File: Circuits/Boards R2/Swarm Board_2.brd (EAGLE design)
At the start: 54.9 x 63.6 mm, 94 parts, among them CON1 ISP(2X3), CON2 MAIN_CONNECTOR, CON3 FTDI_3PIN, CON4 HEADER_3X1, T1 NPN2N2222, T10 TEFT4300, T11 NPN2N2222, T13 NPN2N2222, T14 NPN2N2222, T15 NPN2N2222, T16 NPN2N2222, T17 NPN2N2222, T18 NPN2N2222, T2 NPN2N2222, T3 NPN2N2222, T4 TEFT4300, T5 TEFT4300, T6 TEFT4300, T7 TEFT4300, T8 TEFT4300, T9 TEFT4300, U1 ATMEGA324P, U2 MCP73833

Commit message: more board updates
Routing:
- net +3V: track 376.1 -> 375.4 mm
- net +VRAW: track 85.2 -> 85.7 mm
- net +VCHG: track 44.9 -> 45.4 mm
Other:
- board size 54.9 x 63.6 mm -> 56.1 x 63.5 mm
- board text added: "11-26-12"
- board text removed: "10-28-12"
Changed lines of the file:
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@@
 <board>
 <plain>
-<wire x1="4.318" y1="47.625" x2="4.318" y2="15.7988" width="0.2032" layer="20"/>
-<wire x1="59.182" y1="47.625" x2="59.182" y2="15.7988" width="0.2032" layer="20"/>
+<wire x1="3.716528125" y1="46.6557375" x2="3.716528125" y2="16.8442625" width="0.2032" layer="20"/>
+<wire x1="59.783471875" y1="46.6557375" x2="59.783471875" y2="16.8442625" width="0.2032" layer="20"/>
 <text x="43.434" y="31.496" size="0.8128" layer="21">RXI</text>
 <text x="43.307" y="34.036" size="0.8128" layer="21">TXO</text>
@@
 <text x="43.307" y="49.022" size="0.6096" layer="21">DATA</text>
 <text x="17.907" y="32.512" size="1.016" layer="21" rot="R90">CHGSTATUS</text>
-<text x="14.097" y="9.144" size="1.27" layer="21">10-28-12</text>
+<text x="14.097" y="9.144" size="1.27" layer="21">11-26-12</text>
 <text x="10.541" y="11.684" size="1.27" layer="21">SwarmBoard V2</text>
 <text x="17.653" y="6.731" size="1.27" layer="21">CPRC</text>
-<wire x1="4.318" y1="47.625" x2="59.182" y2="47.625" width="0.2032" layer="20" curve="-120"/>
-<wire x1="4.318" y1="15.748" x2="59.182" y2="15.748" width="0.2032" layer="20" curve="120"/>
+<wire x1="3.716528125" y1="46.6557375" x2="59.783471875" y2="46.6557375" width="0.2032" layer="20" curve="-124"/>
+<wire x1="3.716528125" y1="16.8442625" x2="59.783471875" y2="16.8442625" width="0.2032" layer="20" curve="124"/>
 <text x="27.051" y="48.387" size="0.8128" layer="22" rot="MR270">B+</text>
 <text x="27.178" y="42.164" size="0.8128" layer="22" rot="MR270">B-</text>
@@
 </class>
 </classes>
-<designrules name="default">
+<designrules name="SparkFunDRC">
 <description language="en">&lt;b&gt;EAGLE Design Rules&lt;/b&gt;
 &lt;p&gt;
@@
 <wire x1="58.039" y1="27.178" x2="58.039" y2="20.066" width="0.4064" layer="16"/>
 <wire x1="58.039" y1="20.066" x2="58.039" y2="15.875" width="0.4064" layer="16"/>
-<wire x1="58.039" y1="15.875" x2="46.355" y2="4.191" width="0.4064" layer="16"/>
-<wire x1="46.355" y1="4.191" x2="33.02" y2="4.064" width="0.4064" layer="16"/>
-<wire x1="33.02" y1="4.064" x2="17.399" y2="4.064" width="0.4064" layer="16"/>
-<wire x1="17.399" y1="4.064" x2="5.7785" y2="15.6845" width="0.4064" layer="16"/>
+<wire x1="58.039" y1="15.875" x2="46.609" y2="4.445" width="0.4064" layer="16"/>
+<wire x1="46.609" y1="4.445" x2="33.02" y2="4.445" width="0.4064" layer="16"/>
+<wire x1="33.02" y1="4.445" x2="17.018" y2="4.445" width="0.4064" layer="16"/>
+<wire x1="17.018" y1="4.445" x2="5.7785" y2="15.6845" width="0.4064" layer="16"/>
 <wire x1="5.7785" y1="15.6845" x2="5.461" y2="16.129" width="0.4064" layer="16"/>
 <wire x1="5.461" y1="16.129" x2="5.461" y2="26.924" width="0.4064" layer="16"/>
@@
 <wire x1="30.722" y1="8.255" x2="32.377" y2="6.35" width="0.254" layer="1"/>
 <wire x1="32.377" y1="6.35" x2="33.02" y2="6.35" width="0.254" layer="1"/>
-<wire x1="33.02" y1="6.35" x2="33.02" y2="4.064" width="0.4064" layer="16"/>
+<wire x1="33.02" y1="6.35" x2="33.02" y2="4.445" width="0.4064" layer="16"/>
 <wire x1="12.4206" y1="22.05485" x2="10.916" y2="20.940478125" width="0.254" layer="1"/>
 <wire x1="10.16" y1="18.542" x2="10.916" y2="20.940478125" width="0.254" layer="1"/>
@@
 <wire x1="10.533" y1="39.616" x2="11.049" y2="39.612" width="0.254" layer="1"/>
 <wire x1="11.049" y1="39.612" x2="12.954" y2="39.612" width="0.254" layer="1"/>
-<wire x1="18.415" y1="26.602" x2="17.2085" y2="26.6065" width="0.4064" layer="1"/>
-<via x="17.2085" y="26.6065" extent="1-16" drill="0.508"/>
+<wire x1="18.415" y1="26.602" x2="17.4625" y2="26.6065" width="0.4064" layer="1"/>
+<via x="17.4625" y="26.6065" extent="1-16" drill="0.508"/>
 <wire x1="18.415" y1="26.602" x2="18.415" y2="28.841" width="0.4064" layer="1"/>
 <contactref element="U$1" pad="18"/>
@@
 <wire x1="16.51" y1="38.227" x2="15.629" y2="39.108" width="0.4064" layer="1"/>
 <wire x1="15.629" y1="39.108" x2="14.859" y2="39.108" width="0.4064" layer="1"/>
-<wire x1="16.155" y1="34.163" x2="18.669" y2="34.163" width="0.4064" layer="1"/>
-<wire x1="18.669" y1="34.163" x2="19.177" y2="34.671" width="0.4064" layer="1"/>
-<wire x1="19.177" y1="34.671" x2="19.177" y2="35.814" width="0.4064" layer="1"/>
-<wire x1="19.177" y1="35.814" x2="18.542" y2="36.449" width="0.4064" layer="1"/>
-<wire x1="18.542" y1="36.449" x2="16.51" y2="36.449" width="0.4064" layer="1"/>
+<wire x1="16.155" y1="34.163" x2="18.923" y2="34.163" width="0.4064" layer="1"/>
+<wire x1="18.923" y1="34.163" x2="19.431" y2="34.671" width="0.4064" layer="1"/>
+<wire x1="19.431" y1="34.671" x2="19.431" y2="35.814" width="0.4064" layer="1"/>
+<wire x1="19.431" y1="35.814" x2="18.796" y2="36.449" width="0.4064" layer="1"/>
+<wire x1="18.796" y1="36.449" x2="16.51" y2="36.449" width="0.4064" layer="1"/>
 <wire x1="14.325" y1="34.813" x2="14.325" y2="35.28" width="0.4064" layer="1"/>
 <wire x1="14.325" y1="35.28" x2="14.605" y2="35.56" width="0.4064" layer="1"/>
@@
 <wire x1="12.827" y1="45.847" x2="15.875" y2="45.847" width="0.254" layer="1"/>
 <wire x1="15.875" y1="45.847" x2="15.875" y2="50.769025" width="0.254" layer="1"/>
-<wire x1="21.082" y1="32.258" x2="19.939" y2="33.401" width="0.254" layer="1"/>
-<wire x1="19.939" y1="33.401" x2="19.939" y2="36.449" width="0.254" layer="1"/>
-<wire x1="19.939" y1="36.449" x2="19.05" y2="37.338" width="0.254" layer="1"/>
-<wire x1="19.05" y1="37.338" x2="19.05" y2="43.307" width="0.254" layer="1"/>
+<wire x1="21.082" y1="32.258" x2="20.066" y2="33.274" width="0.254" layer="1"/>
+<wire x1="20.066" y1="33.274" x2="20.066" y2="42.291" width="0.254" layer="1"/>
+<wire x1="20.066" y1="42.291" x2="19.05" y2="43.307" width="0.254" layer="1"/>
 <wire x1="19.05" y1="43.307" x2="16.51" y2="45.847" width="0.254" layer="16"/>
 <via x="16.51" y="45.847" extent="1-16" drill="0.508"/>
@@
 <wire x1="16.155" y1="34.813" x2="15.517" y2="34.813" width="0.4064" layer="1"/>
 <wire x1="15.517" y1="34.813" x2="15.24" y2="34.663" width="0.254" layer="1"/>
-<wire x1="16.155" y1="33.513" x2="17.548" y2="33.513" width="0.4064" layer="1"/>
-<wire x1="17.548" y1="33.513" x2="18.0375" y2="33.0235" width="0.4064" layer="1"/>
-<wire x1="16.155" y1="34.813" x2="17.541" y2="34.813" width="0.4064" layer="1"/>
-<wire x1="17.541" y1="34.813" x2="18.034" y2="35.306" width="0.4064" layer="1"/>
-<via x="18.034" y="35.306" extent="1-16" drill="0.508"/>
-<wire x1="18.034" y1="35.306" x2="18.0375" y2="34.4135" width="0.4064" layer="16"/>
-<wire x1="18.0375" y1="34.4135" x2="18.0375" y2="33.0235" width="0.4064" layer="16"/>
-<via x="18.0375" y="33.0235" extent="1-16" drill="0.508"/>
-<via x="18.034" y="37.592" extent="1-16" drill="0.508"/>
-<wire x1="18.034" y1="35.306" x2="18.034" y2="37.592" width="0.4064" layer="16"/>
+<wire x1="16.155" y1="33.513" x2="17.802" y2="33.513" width="0.4064" layer="1"/>
+<wire x1="17.802" y1="33.513" x2="18.2915" y2="33.0235" width="0.4064" layer="1"/>
+<wire x1="16.155" y1="34.813" x2="17.795" y2="34.813" width="0.4064" layer="1"/>
+<wire x1="17.795" y1="34.813" x2="18.288" y2="35.306" width="0.4064" layer="1"/>
+<via x="18.288" y="35.306" extent="1-16" drill="0.508"/>
+<wire x1="18.288" y1="35.306" x2="18.2915" y2="34.4135" width="0.4064" layer="16"/>
+<wire x1="18.2915" y1="34.4135" x2="18.2915" y2="33.0235" width="0.4064" layer="16"/>
+<via x="18.2915" y="33.0235" extent="1-16" drill="0.508"/>
+<via x="18.288" y="37.592" extent="1-16" drill="0.508"/>
+<wire x1="18.288" y1="35.306" x2="18.288" y2="37.592" width="0.4064" layer="16"/>
 <wire x1="15.621" y1="41.529" x2="23.622" y2="49.53" width="0.4064" layer="1"/>
-<wire x1="18.034" y1="37.592" x2="18.034" y2="37.846" width="0.4064" layer="1"/>
-<wire x1="18.034" y1="37.846" x2="15.621" y2="40.259" width="0.4064" layer="1"/>
+<wire x1="18.288" y1="37.592" x2="15.621" y2="40.259" width="0.4064" layer="1"/>
 <wire x1="15.621" y1="40.259" x2="15.621" y2="41.529" width="0.4064" layer="1"/>
 <wire x1="23.622" y1="49.53" x2="32.385" y2="49.53" width="0.4064" layer="1"/>
 <wire x1="32.385" y1="49.53" x2="33.528" y2="50.673" width="0.4064" layer="1"/>
 <wire x1="33.528" y1="50.673" x2="39.497" y2="50.673" width="0.4064" layer="1"/>
-<wire x1="18.415" y1="30.341" x2="18.034" y2="30.741" width="0.4064" layer="1"/>
-<wire x1="18.034" y1="30.741" x2="18.0375" y2="33.0235" width="0.4064" layer="1"/>
+<wire x1="18.415" y1="30.341" x2="18.288" y2="30.487" width="0.4064" layer="1"/>
+<wire x1="18.288" y1="30.487" x2="18.2915" y2="33.0235" width="0.4064" layer="1"/>
 <contactref element="U$1" pad="13"/>
 <contactref element="U$1" pad="24"/>

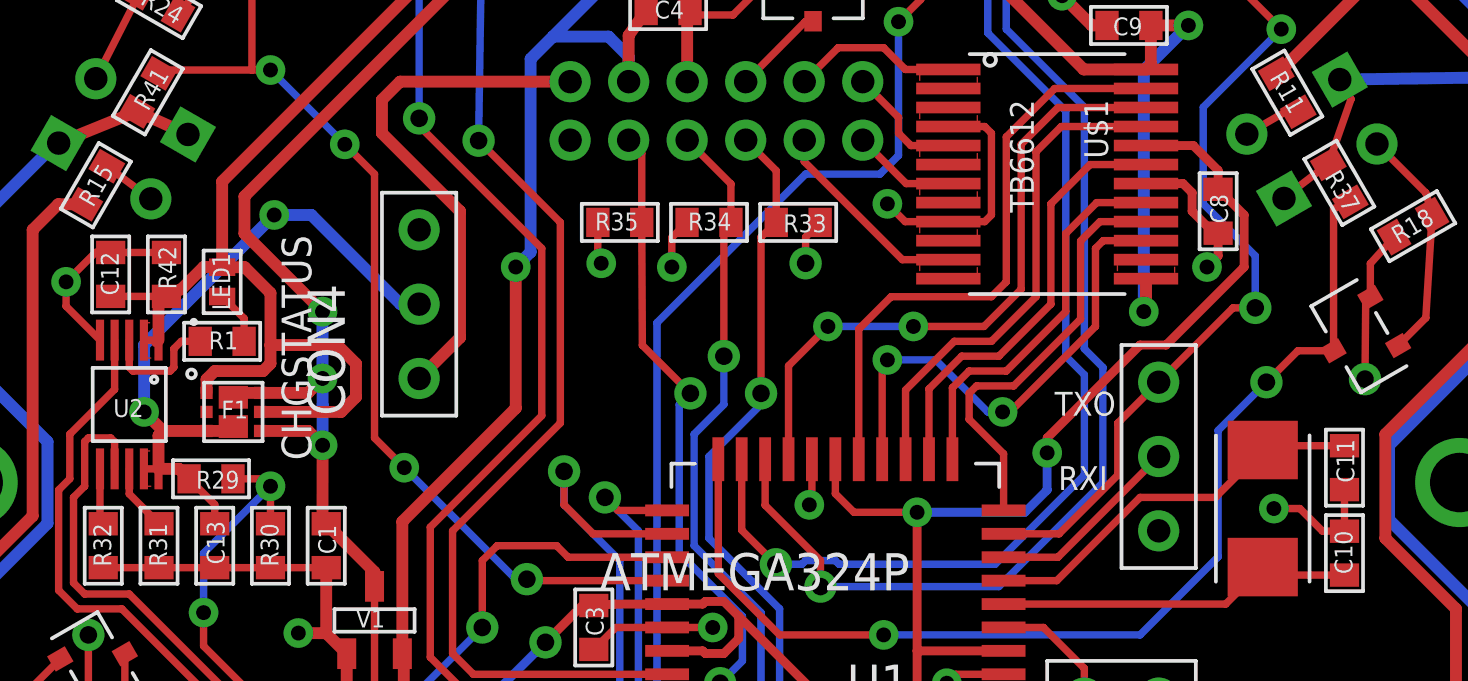
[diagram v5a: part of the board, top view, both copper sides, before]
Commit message: fixed led on swarm board
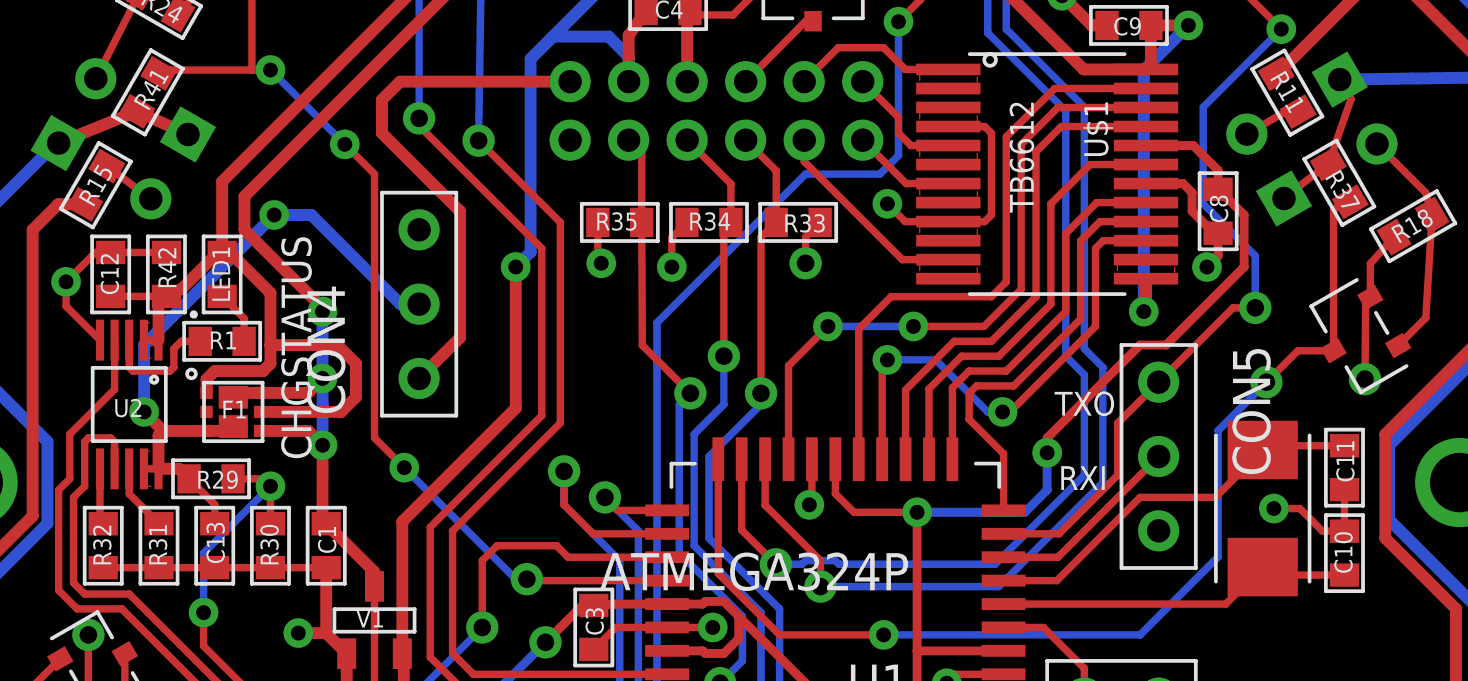
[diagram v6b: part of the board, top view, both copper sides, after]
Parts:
- CON5: value FTDI_3PIN -> HEADER_3X1
- moved LED1 0.25 mm to (14.9, 38.9)
- renumbered CON3 to CON5
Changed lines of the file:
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@@
 <?xml version="1.0" encoding="utf-8"?>
 <!DOCTYPE eagle SYSTEM "eagle.dtd">
-<eagle version="6.3">
+<eagle version="6.2">
 <drawing>
 <settings>
@@
 </class>
 </classes>
-<designrules name="SparkFunDRC">
+<designrules>
 <description language="en">&lt;b&gt;EAGLE Design Rules&lt;/b&gt;
 &lt;p&gt;
@@
 <attribute name="VALUE" x="35.75" y="40.45" size="0.8128" layer="28" rot="MR0"/>
 </element>
-<element name="CON3" library="Mechanical" package="3PINHEADER_.100&quot;" value="FTDI_3PIN" x="46.863" y="32.639" smashed="yes" rot="R270">
-<attribute name="VALUE" x="43.053" y="36.449" size="1.27" layer="27" rot="R270"/>
-</element>
 <element name="T10" library="Passive" package="3MM_LED_RA" value="TEFT4300" x="27.94" y="57.15" smashed="yes"/>
 <element name="R27" library="Passive" package="0603" value="10k" x="30.734" y="55.499" smashed="yes" rot="R270">
@@
 <attribute name="VALUE" x="11.684" y="39.932" size="0.4064" layer="27" rot="R270"/>
 </element>
-<element name="LED1" library="Passive" package="LED0603" value="red" x="14.859" y="38.608" smashed="yes" rot="R90">
-<attribute name="NAME" x="15.132" y="37.638" size="0.6096" layer="25" rot="R90"/>
-<attribute name="VALUE" x="16.129" y="37.538" size="0.4064" layer="27" rot="R90"/>
+<element name="LED1" library="Passive" package="LED0603" value="red" x="14.859" y="38.862" smashed="yes" rot="R90">
+<attribute name="NAME" x="15.132" y="37.892" size="0.6096" layer="25" rot="R90"/>
+<attribute name="VALUE" x="16.129" y="37.792" size="0.4064" layer="27" rot="R90"/>
 </element>
 <element name="R1" library="Passive" package="0603" value="1.5k" x="14.859" y="36.576" smashed="yes">
@@
 <element name="R4" library="Passive" package="0603" value="70" x="21.717" y="17.399" rot="R180"/>
 <element name="R5" library="Passive" package="0603" value="70" x="21.717" y="15.621" rot="R180"/>
+<element name="CON5" library="Mechanical" package="3PINHEADER_.100&quot;" value="HEADER_3X1" x="46.863" y="32.639" rot="R270"/>
 </elements>
 <signals>
@@
 <contactref element="C2" pad="2"/>
 <contactref element="CON1" pad="3"/>
-<contactref element="CON3" pad="3"/>
 <contactref element="T1" pad="2"/>
 <contactref element="R9" pad="1"/>
@@
 <wire x1="48.895" y1="39.497" x2="48.514" y2="39.116" width="0.3048" layer="1"/>
 <wire x1="44.323" y1="25.4" x2="44.323" y2="24.384" width="0.254" layer="1"/>
+<contactref element="CON5" pad="3"/>
 </signal>
 <signal name="+VBAT">
@@
 <wire x1="12.573" y1="36.506" x2="12.684" y2="36.617" width="0.254" layer="1"/>
 <wire x1="12.684" y1="36.617" x2="12.184" y2="36.617" width="0.254" layer="1"/>
-<wire x1="14.597" y1="39.108" x2="14.859" y2="39.108" width="0.254" layer="1"/>
+<wire x1="14.851" y1="39.616" x2="14.859" y2="39.612" width="0.254" layer="1"/>
 <wire x1="23.622" y1="50.8" x2="14.859" y2="42.037" width="0.4064" layer="1"/>
-<wire x1="14.859" y1="42.037" x2="14.859" y2="39.108" width="0.4064" layer="1"/>
+<wire x1="14.859" y1="42.037" x2="14.859" y2="39.612" width="0.4064" layer="1"/>
 <polygon width="0.254" layer="1" thermals="no">
 <vertex x="12.192" y="37.211"/>
@@
 </polygon>
 <wire x1="16.51" y1="36.449" x2="16.51" y2="38.227" width="0.4064" layer="1"/>
-<wire x1="16.51" y1="38.227" x2="15.629" y2="39.108" width="0.4064" layer="1"/>
-<wire x1="15.629" y1="39.108" x2="14.859" y2="39.108" width="0.4064" layer="1"/>
+<wire x1="16.51" y1="38.227" x2="15.121" y2="39.616" width="0.4064" layer="1"/>
+<wire x1="15.121" y1="39.616" x2="14.859" y2="39.612" width="0.4064" layer="1"/>
 <wire x1="16.155" y1="34.163" x2="18.923" y2="34.163" width="0.4064" layer="1"/>
 <wire x1="18.923" y1="34.163" x2="19.431" y2="34.671" width="0.4064" layer="1"/>
@@
 <wire x1="11.049" y1="38.112" x2="12.954" y2="38.112" width="0.254" layer="1"/>
 <wire x1="12.954" y1="38.112" x2="13.47" y2="38.362" width="0.4064" layer="1"/>
-<wire x1="13.47" y1="38.362" x2="14.224" y2="39.116" width="0.4064" layer="1"/>
-<wire x1="14.224" y1="39.116" x2="14.851" y2="39.116" width="0.4064" layer="1"/>
-<wire x1="14.851" y1="39.116" x2="14.859" y2="39.108" width="0.254" layer="1"/>
+<wire x1="13.47" y1="38.362" x2="14.605" y2="39.497" width="0.4064" layer="1"/>
+<wire x1="14.605" y1="39.497" x2="14.724" y2="39.497" width="0.4064" layer="1"/>
+<wire x1="14.724" y1="39.497" x2="14.859" y2="39.612" width="0.254" layer="1"/>
 <wire x1="12.954" y1="38.112" x2="12.684" y2="38.092" width="0.4064" layer="1"/>
 <wire x1="12.684" y1="38.092" x2="12.684" y2="36.617" width="0.4064" layer="1"/>
@@
 <signal name="DATAANTENNA">
 <contactref element="U1" pad="10"/>
-<contactref element="CON3" pad="1"/>
 <contactref element="ANT2" pad="P$1"/>
 <wire x1="41.564" y1="29.997" x2="43.459" y2="29.997" width="0.254" layer="1"/>
@@
 <wire x1="43.459" y1="29.997" x2="45.466" y2="32.004" width="0.254" layer="1"/>
 <wire x1="45.466" y1="32.004" x2="45.466" y2="33.782" width="0.254" layer="1"/>
+<via x="50.165" y="37.719" extent="1-16" drill="0.6"/>
+<wire x1="50.165" y1="37.719" x2="49.657" y2="37.719" width="0.254" layer="1"/>
+<contactref element="CON5" pad="1"/>
 <wire x1="45.466" y1="33.782" x2="46.863" y2="35.179" width="0.254" layer="1"/>
-<via x="50.165" y="37.719" extent="1-16" drill="0.6"/>
-<wire x1="50.165" y1="37.719" x2="49.403" y2="37.719" width="0.254" layer="1"/>
-<wire x1="49.403" y1="37.719" x2="46.863" y2="35.179" width="0.254" layer="1"/>
+<wire x1="46.863" y1="35.179" x2="49.403" y2="37.719" width="0.254" layer="1"/>
+<wire x1="49.403" y1="37.719" x2="49.657" y2="37.719" width="0.254" layer="1"/>
 </signal>
 <signal name="N$8">
 <contactref element="U1" pad="9"/>
-<contactref element="CON3" pad="2"/>
 <wire x1="41.564" y1="29.197" x2="43.421" y2="29.197" width="0.254" layer="1"/>
+<contactref element="CON5" pad="2"/>
 <wire x1="43.421" y1="29.197" x2="46.863" y2="32.639" width="0.254" layer="1"/>
 </signal>
@@
 <wire x1="18.288" y1="35.306" x2="18.288" y2="37.592" width="0.4064" layer="16"/>
 <wire x1="15.621" y1="41.529" x2="23.622" y2="49.53" width="0.4064" layer="1"/>
-<wire x1="18.288" y1="37.592" x2="15.621" y2="40.259" width="0.4064" layer="1"/>
-<wire x1="15.621" y1="40.259" x2="15.621" y2="41.529" width="0.4064" layer="1"/>
+<wire x1="15.621" y1="40.386" x2="15.621" y2="41.529" width="0.4064" layer="1"/>
 <wire x1="23.622" y1="49.53" x2="32.385" y2="49.53" width="0.4064" layer="1"/>
 <wire x1="32.385" y1="49.53" x2="33.528" y2="50.673" width="0.4064" layer="1"/>
@@
 <wire x1="20.066" y1="28.201" x2="20.066" y2="21.844" width="0.254" layer="1"/>
 <wire x1="20.066" y1="21.844" x2="20.701" y2="21.209" width="0.254" layer="1"/>
+<wire x1="15.621" y1="40.386" x2="18.288" y2="37.719" width="0.4064" layer="1"/>
+<wire x1="18.288" y1="37.719" x2="18.288" y2="37.592" width="0.4064" layer="1"/>
 </signal>
 <signal name="N$1">
@@
 <contactref element="LED1" pad="1"/>
 <wire x1="15.609" y1="36.576" x2="15.609" y2="37.358" width="0.254" layer="1"/>
-<wire x1="15.609" y1="37.358" x2="14.859" y2="38.108" width="0.254" layer="1"/>
+<wire x1="15.609" y1="37.358" x2="14.859" y2="38.112" width="0.254" layer="1"/>
 </signal>
 <signal name="N$4">

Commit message: slight updates to part values to account for availibility
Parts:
- R29: value 7k -> 7.5k
- R3: value 180 -> 200
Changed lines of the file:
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@@
 <attribute name="VALUE" x="13.184" y="38.417" size="0.6096" layer="27" rot="R180"/>
 </element>
-<element name="R29" library="Passive" package="0603" value="7k" x="14.478" y="31.877" smashed="yes" rot="R180">
+<element name="R29" library="Passive" package="0603" value="7.5k" x="14.478" y="31.877" smashed="yes" rot="R180">
 <attribute name="NAME" x="15.448" y="32.15" size="0.6096" layer="25" rot="R180"/>
 <attribute name="VALUE" x="15.548" y="33.147" size="0.4064" layer="27" rot="R180"/>
@@
 <element name="CON4" library="Mechanical" package="3PINHEADER_.100&quot;" value="HEADER_3X1" x="21.59" y="37.846" rot="R90"/>
 <element name="LED10" library="Passive" package="PLCC4" value="SMD_RGB" x="16.637" y="16.764" rot="R270"/>
-<element name="R3" library="Passive" package="0603" value="180" x="21.717" y="13.843" rot="R180"/>
+<element name="R3" library="Passive" package="0603" value="200" x="21.717" y="13.843" rot="R180"/>
 <element name="R4" library="Passive" package="0603" value="70" x="21.717" y="17.399" rot="R180"/>
 <element name="R5" library="Passive" package="0603" value="70" x="21.717" y="15.621" rot="R180"/>
